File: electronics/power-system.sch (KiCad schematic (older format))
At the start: 43 parts

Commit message: Replace 3V3 switching regulator with 5V version
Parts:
- removed D?: 1N5822, symbol Device:D_Schottky
- C?: value 100u -> 120u; symbol Device:C_Small -> Device:CP_Small
- C?: value 1000u -> 470u
- D?: value 1N5822 -> SB520
- U?: value LM2576S-3.3 -> LM2576T-5; symbol Regulator_Switching:LM2576S-3.3 -> Regulator_Switching:LM2576T-5
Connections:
- net +3V3 renamed +5V
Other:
- note added: "5V Switching regulator (3A max output)"
- note removed: "Supplementary 3.3v regulator for high current demand 3.3v circuitry"
- moved on the sheet: C?
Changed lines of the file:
@@
 	7400 1550 7500 1550
 $Comp
-L Regulator_Switching:LM2576S-3.3 U?
+L Regulator_Switching:LM2576T-5 U?
 U 1 1 611D8913
 P 6150 3950
@@
 AR Path="/611ADD88/611D8913" Ref="U?"  Part="1"
 F 0 "U?" H 5750 4200 50  0000 L CNN
-F 1 "LM2576S-3.3" H 6150 4200 50  0000 L CNN
+F 1 "LM2576T-5" H 6150 4200 50  0000 L CNN
 F 2 "Package_TO_SOT_SMD:TO-263-5_TabPin3" H 6150 3700 50  0001 L CIN
 F 3 "http://www.ti.com/lit/ds/symlink/lm2576.pdf" H 6150 3950 50  0001 C CNN
@@
 $EndComp
 $Comp
-L Device:C_Small C?
+L Device:CP_Small C?
 U 1 1 611D8919
-P 5300 4000
+P 5300 4100
 AR Path="/611D8919" Ref="C?"  Part="1"
 AR Path="/611ADD88/611D8919" Ref="C?"  Part="1"
-F 0 "C?" H 5310 4070 50  0000 L CNN
-F 1 "100u" H 5310 3920 50  0000 L CNN
-F 2 "" H 5300 4000 50  0001 C CNN
-F 3 "~" H 5300 4000 50  0001 C CNN
-	1    5300 4000
+F 0 "C?" H 5310 4170 50  0000 L CNN
+F 1 "120u" H 5310 4020 50  0000 L CNN
+F 2 "" H 5300 4100 50  0001 C CNN
+F 3 "~" H 5300 4100 50  0001 C CNN
+	1    5300 4100
 	1    0    0    -1
 $EndComp
@@
 	5650 3850 5300 3850
 Wire Wire Line
-	5300 3850 5300 3900
+	5300 3850 5300 4000
 Connection ~ 5300 3850
 Wire Wire Line
-	5300 4100 5300 4350
+	5300 4200 5300 4350
 $Comp
 L power:GND1 #PWR?
@@
 	6650 4050 6750 4050
 Wire Wire Line
-	7200 3850 6650 3850
+	7250 3850 6650 3850
 $Comp
 L Device:D_Schottky D?
@@
 AR Path="/611ADD88/611D8937" Ref="D?"  Part="1"
 F 0 "D?" H 6750 4300 50  0000 C CNN
-F 1 "1N5822" H 6750 4100 50  0000 C CNN
+F 1 "SB520" H 6800 4100 50  0000 C CNN
 F 2 "" H 6750 4200 50  0001 C CNN
 F 3 "~" H 6750 4200 50  0001 C CNN
@@
 L Device:CP_Small C?
 U 1 1 611D894E
-P 7200 4200
+P 7250 4200
 AR Path="/611D894E" Ref="C?"  Part="1"
 AR Path="/611ADD88/611D894E" Ref="C?"  Part="1"
-F 0 "C?" H 7210 4270 50  0000 L CNN
-F 1 "1000u" H 7210 4120 50  0000 L CNN
-F 2 "" H 7200 4200 50  0001 C CNN
-F 3 "~" H 7200 4200 50  0001 C CNN
-	1    7200 4200
+F 0 "C?" H 7260 4270 50  0000 L CNN
+F 1 "470u" H 7260 4120 50  0000 L CNN
+F 2 "" H 7250 4200 50  0001 C CNN
+F 3 "~" H 7250 4200 50  0001 C CNN
+	1    7250 4200
 	1    0    0    -1
 $EndComp
 Wire Wire Line
-	7200 4100 7200 4050
-Connection ~ 7200 3850
+	7250 4100 7250 4050
+Connection ~ 7250 3850
 $Comp
 L power:GND1 #PWR?
 U 1 1 611D8956
-P 7200 4350
+P 7250 4350
 AR Path="/611D8956" Ref="#PWR?"  Part="1"
 AR Path="/611ADD88/611D8956" Ref="#PWR?"  Part="1"
-F 0 "#PWR?" H 7200 4100 50  0001 C CNN
-F 1 "GND1" H 7200 4200 50  0000 C CNN
-F 2 "" H 7200 4350 50  0001 C CNN
-F 3 "" H 7200 4350 50  0001 C CNN
-	1    7200 4350
+F 0 "#PWR?" H 7250 4100 50  0001 C CNN
+F 1 "GND1" H 7250 4200 50  0000 C CNN
+F 2 "" H 7250 4350 50  0001 C CNN
+F 3 "" H 7250 4350 50  0001 C CNN
+	1    7250 4350
 	1    0    0    -1
 $EndComp
 Wire Wire Line
-	7200 4350 7200 4300
+	7250 4350 7250 4300
 Wire Wire Line
-	7200 3850 7450 3850
+	7250 3850 7450 3850
 $Comp
 L power:+BATT #PWR?
@@
 	5200 3850 5300 3850
 $Comp
-L power:+3V3 #PWR?
+L power:+5V #PWR?
 U 1 1 611D8966
 P 7450 3750
@@
 AR Path="/611ADD88/611D8966" Ref="#PWR?"  Part="1"
 F 0 "#PWR?" H 7450 3600 50  0001 C CNN
-F 1 "+3V3" H 7450 3890 50  0000 C CNN
+F 1 "+5V" H 7450 3890 50  0000 C CNN
 F 2 "" H 7450 3750 50  0001 C CNN
 F 3 "" H 7450 3750 50  0001 C CNN
@@
 Wire Wire Line
 	7450 3850 7450 3750
-$Comp
-L power:+3.3VP #PWR?
-U 1 1 611D896D
-P 7750 3750
-AR Path="/611D896D" Ref="#PWR?"  Part="1"
-AR Path="/611ADD88/611D896D" Ref="#PWR?"  Part="1"
-F 0 "#PWR?" H 7750 3600 50  0001 C CNN
-F 1 "+3.3VP" H 7750 3890 50  0000 C CNN
-F 2 "" H 7750 3750 50  0001 C CNN
-F 3 "" H 7750 3750 50  0001 C CNN
-	1    7750 3750
-	1    0    0    -1
-$EndComp
-$Comp
-L power:+3V3 #PWR?
-U 1 1 611D8973
-P 8250 3750
-AR Path="/611D8973" Ref="#PWR?"  Part="1"
-AR Path="/611ADD88/611D8973" Ref="#PWR?"  Part="1"
-F 0 "#PWR?" H 8250 3600 50  0001 C CNN
-F 1 "+3V3" H 8250 3890 50  0000 C CNN
-F 2 "" H 8250 3750 50  0001 C CNN
-F 3 "" H 8250 3750 50  0001 C CNN
-	1    8250 3750
-	1    0    0    -1
-$EndComp
-$Comp
-L Device:D_Schottky D?
-U 1 1 611D8979
-P 8000 3850
-AR Path="/611D8979" Ref="D?"  Part="1"
-AR Path="/611ADD88/611D8979" Ref="D?"  Part="1"
-F 0 "D?" H 8000 3950 50  0000 C CNN
-F 1 "1N5822" H 8000 3750 50  0000 C CNN
-F 2 "" H 8000 3850 50  0001 C CNN
-F 3 "~" H 8000 3850 50  0001 C CNN
-	1    8000 3850
-	-1   0    0    1
-$EndComp
 Wire Wire Line
-	7750 3750 7750 3850
+	7150 4050 7250 4050
+Connection ~ 7250 4050
 Wire Wire Line
-	7750 3850 7850 3850
-Wire Wire Line
-	8150 3850 8250 3850
-Wire Wire Line
-	8250 3850 8250 3750
-Wire Wire Line
-	7150 4050 7200 4050
-Connection ~ 7200 4050
-Wire Wire Line
-	7200 4050 7200 3850
+	7250 4050 7250 3850
 Text Notes 5100 3500 0    50   ~ 0
-Supplementary 3.3v regulator for high current demand 3.3v circuitry
+5V Switching regulator (3A max output)
 $Comp
 L crt-smartwatch-symbols:PHV12-0.5K10000P VR?

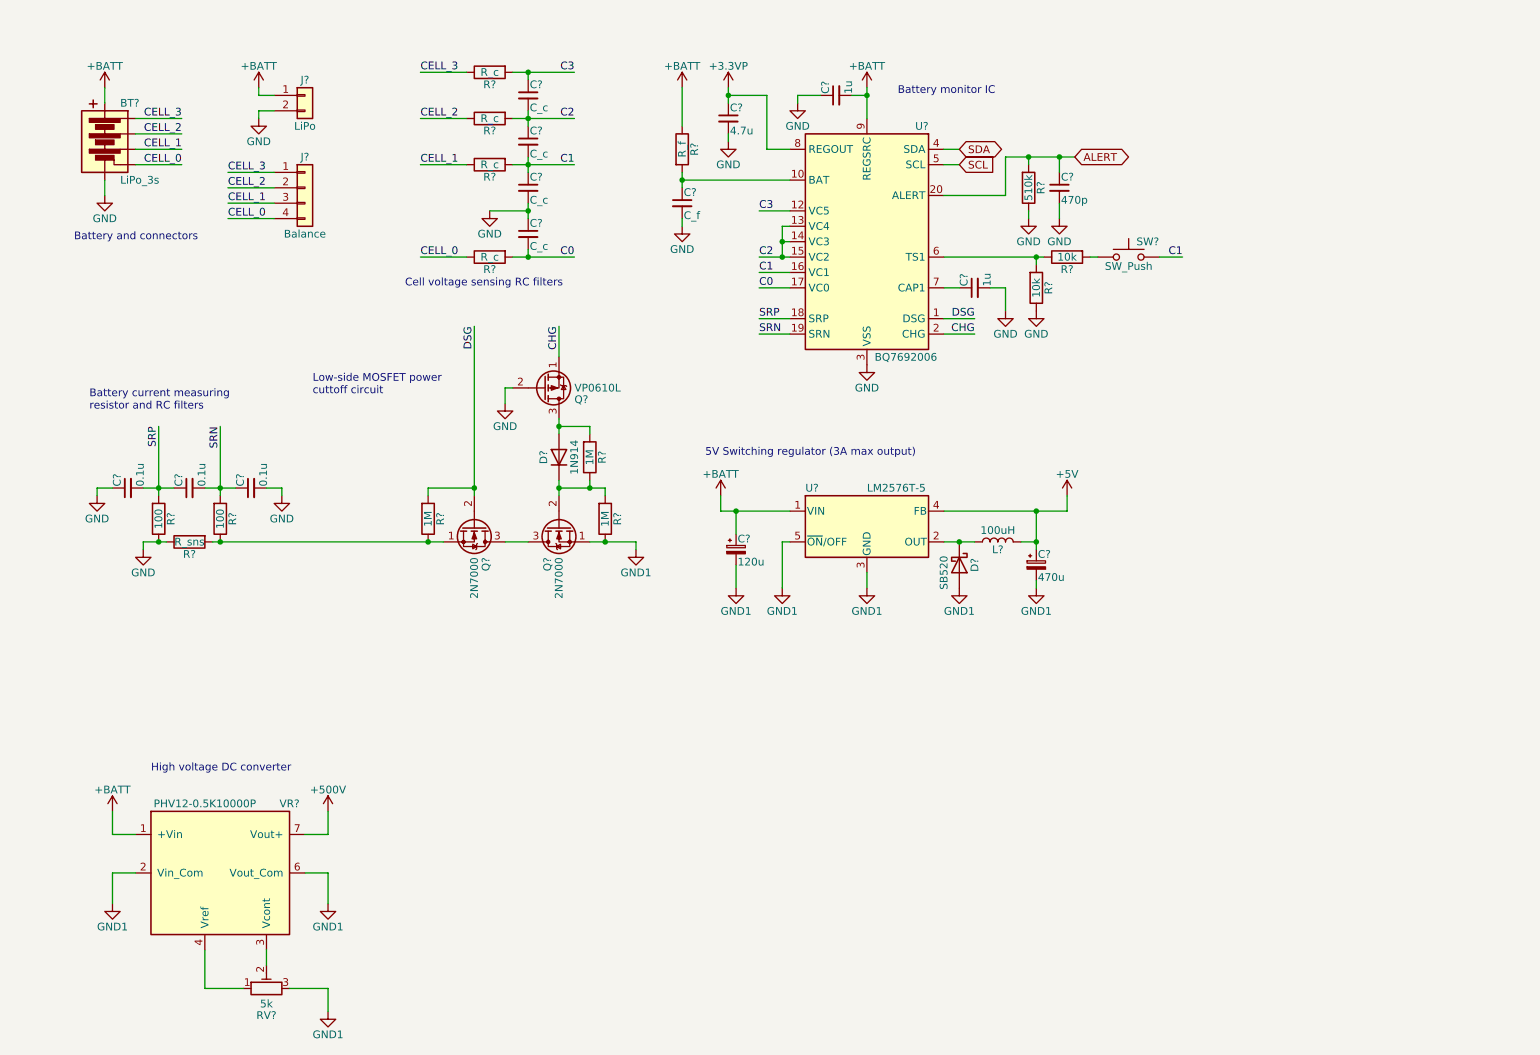
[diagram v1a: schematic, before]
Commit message: Design notes for 3.3V LDR and schematic updates
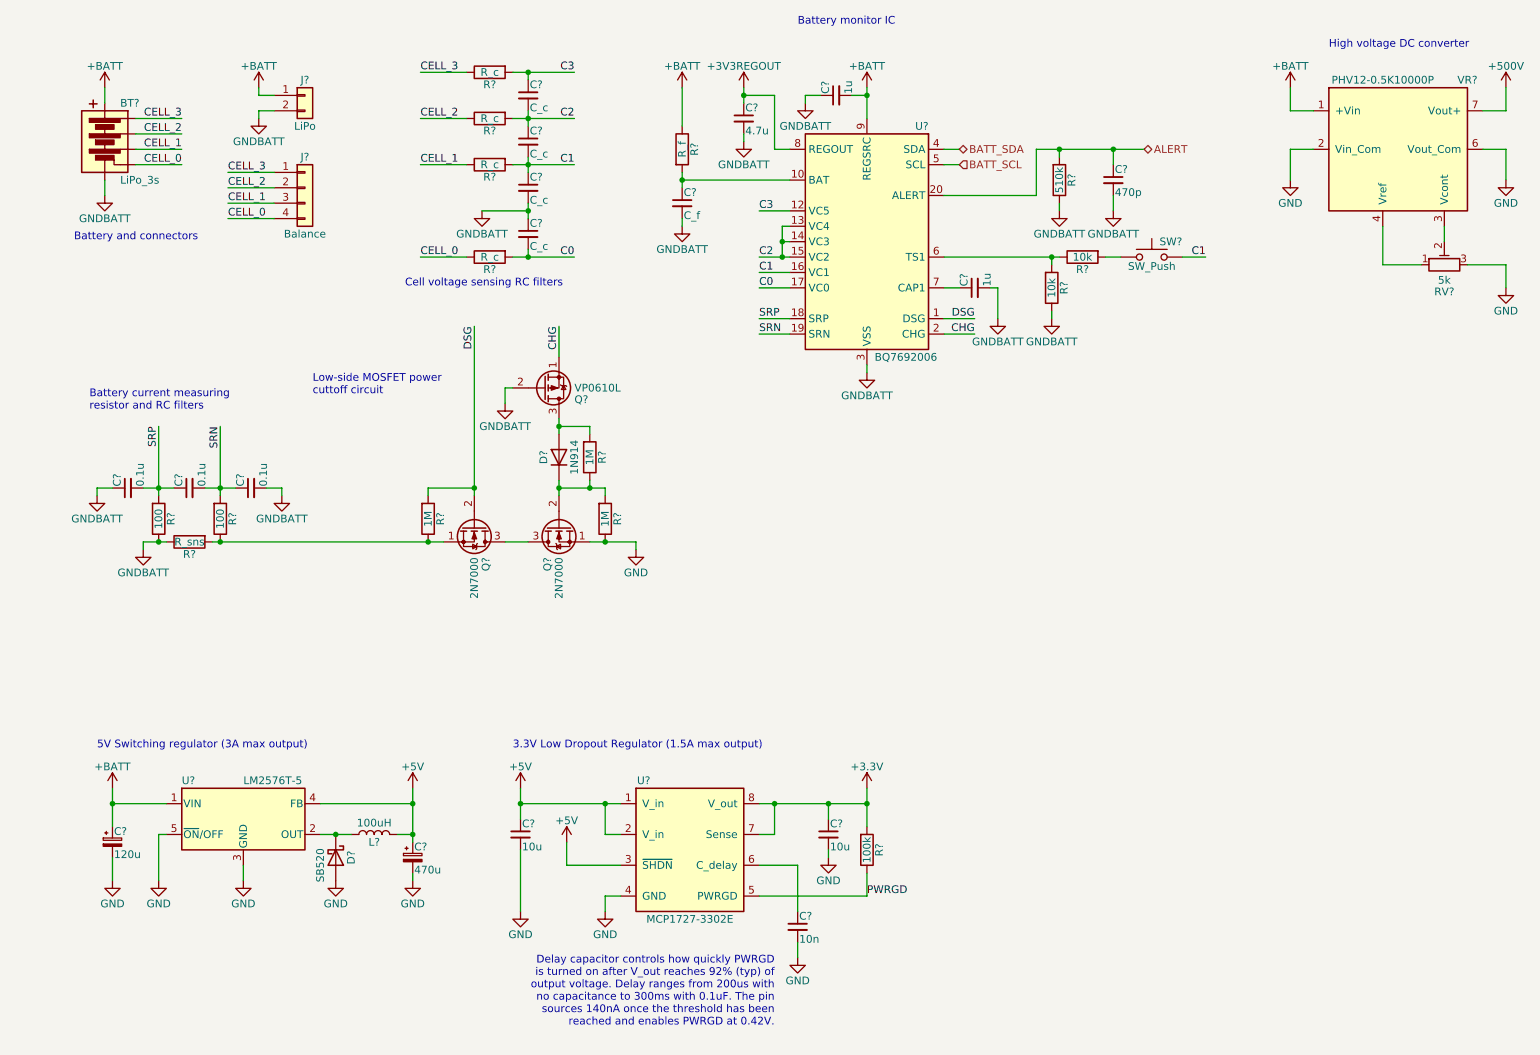
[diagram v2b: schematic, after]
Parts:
- added C? (x2): 10u, symbol Device:C_Small
- added C?: 10n, symbol Device:C_Small
- added R?: 100k, symbol Device:R
- added U?: MCP1727-3302E, symbol crt-smartwatch-symbols:MCP1727-3302E
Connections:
- net GND1 is gone; now on net GND: C?.2, C?.2, D?.2 (A), Q?.1 (S), R?.1, RV?.3, U?.3 (GND), U?.5 (~ON~/OFF), VR?.2 (Vin_Com), VR?.6 (Vout_Com)
- net +5V: now also C?.1, U?.1 (V_in), U?.2 (V_in), U?.3 (~SHDN)
- net GND: now also C?.2, C?.2, C?.2, U?.4 (GND)
- net SCL renamed BATT_SCL
- net SDA renamed BATT_SDA
- new net: C?.1, U?.6 (C_delay)
- new net +3V3: C?.1, R?.2, U?.7 (Sense), U?.8 (V_out)
- new net PWRGD: R?.1, U?.5 (PWRGD)
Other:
- note added: "3.3V Low Dropout Regulator (1.5A max output)"
- note added: "Delay capacitor controls how quickly PWRGD\nis turned on after V_out reaches 92% (typ) of\noutput voltage. Delay ranges from 200us with\nno capacitance to 300ms with 0.1uF. The pin\nsources 140nA once the threshold has been\nreached and enables PWRGD at 0.42V."
- moved on the sheet: C?, D?, L?, R?, RV?, SW?, U?, VR?

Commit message: PIC32 Power Sequencing Microcontroller
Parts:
- added D? (x4): SB520, symbol Device:D_Schottky
- added J?: 12V, symbol Connector_Generic:Conn_01x02
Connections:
- net +BATT: now also J?.2 (Pin_2), D?.1 (K), D?.1 (K), D?.1 (K), D?.1 (K); no longer J?.1 (Pin_1)
- net GND: now also J?.1 (Pin_1), J?.1 (Pin_1); no longer J?.2 (Pin_2)
- new net: D?.2 (A), D?.2 (A), D?.2 (A), D?.2 (A), J?.2 (Pin_2)
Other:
- note added: "Replace with THICC diode\nin final design?"
- moved on the sheet: BT?, J?
